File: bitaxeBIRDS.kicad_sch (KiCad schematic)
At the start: 10 parts, among them J1001 XT30

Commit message: started to piece in the BZM2 into schematic
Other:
- sheet Data ports: added none; removed BAP_VIN
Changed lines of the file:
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@@
-	)
-	(junction
-		(at 78.74 44.45)
-		(diameter 0)
-		(color 0 0 0 0)
 	)
 	(junction
@@
 	(wire
 		(pts
-			(xy 78.74 44.45) (xy 102.87 44.45)
+			(xy 58.42 44.45) (xy 102.87 44.45)
 		)
 		(stroke
@@
 	(wire
 		(pts
-			(xy 58.42 44.45) (xy 78.74 44.45)
-		)
-		(stroke
-			(width 0)
-			(type default)
-		)
-	)
-	(wire
-		(pts
 			(xy 90.17 116.84) (xy 102.87 116.84)
 		)
@@
 		(pts
 			(xy 135.89 100.33) (xy 173.99 100.33)
-		)
-		(stroke
-			(width 0)
-			(type default)
-		)
-	)
-	(wire
-		(pts
-			(xy 78.74 124.46) (xy 102.87 124.46)
-		)
-		(stroke
-			(width 0)
-			(type default)
-		)
-	)
-	(wire
-		(pts
-			(xy 78.74 44.45) (xy 78.74 124.46)
 		)
 		(stroke
@@
 			)
 		)
-		(pin "SDA" input
+		(pin "SDA" bidirectional
 			(at 128.27 100.33 0)
 			(effects
@@
 			(effects
 				(font
-					(size 1.27 1.27)
-				)
-				(justify left)
-			)
-		)
-		(pin "BAP_VIN" input
-			(at 102.87 124.46 180)
-			(effects
-				(font

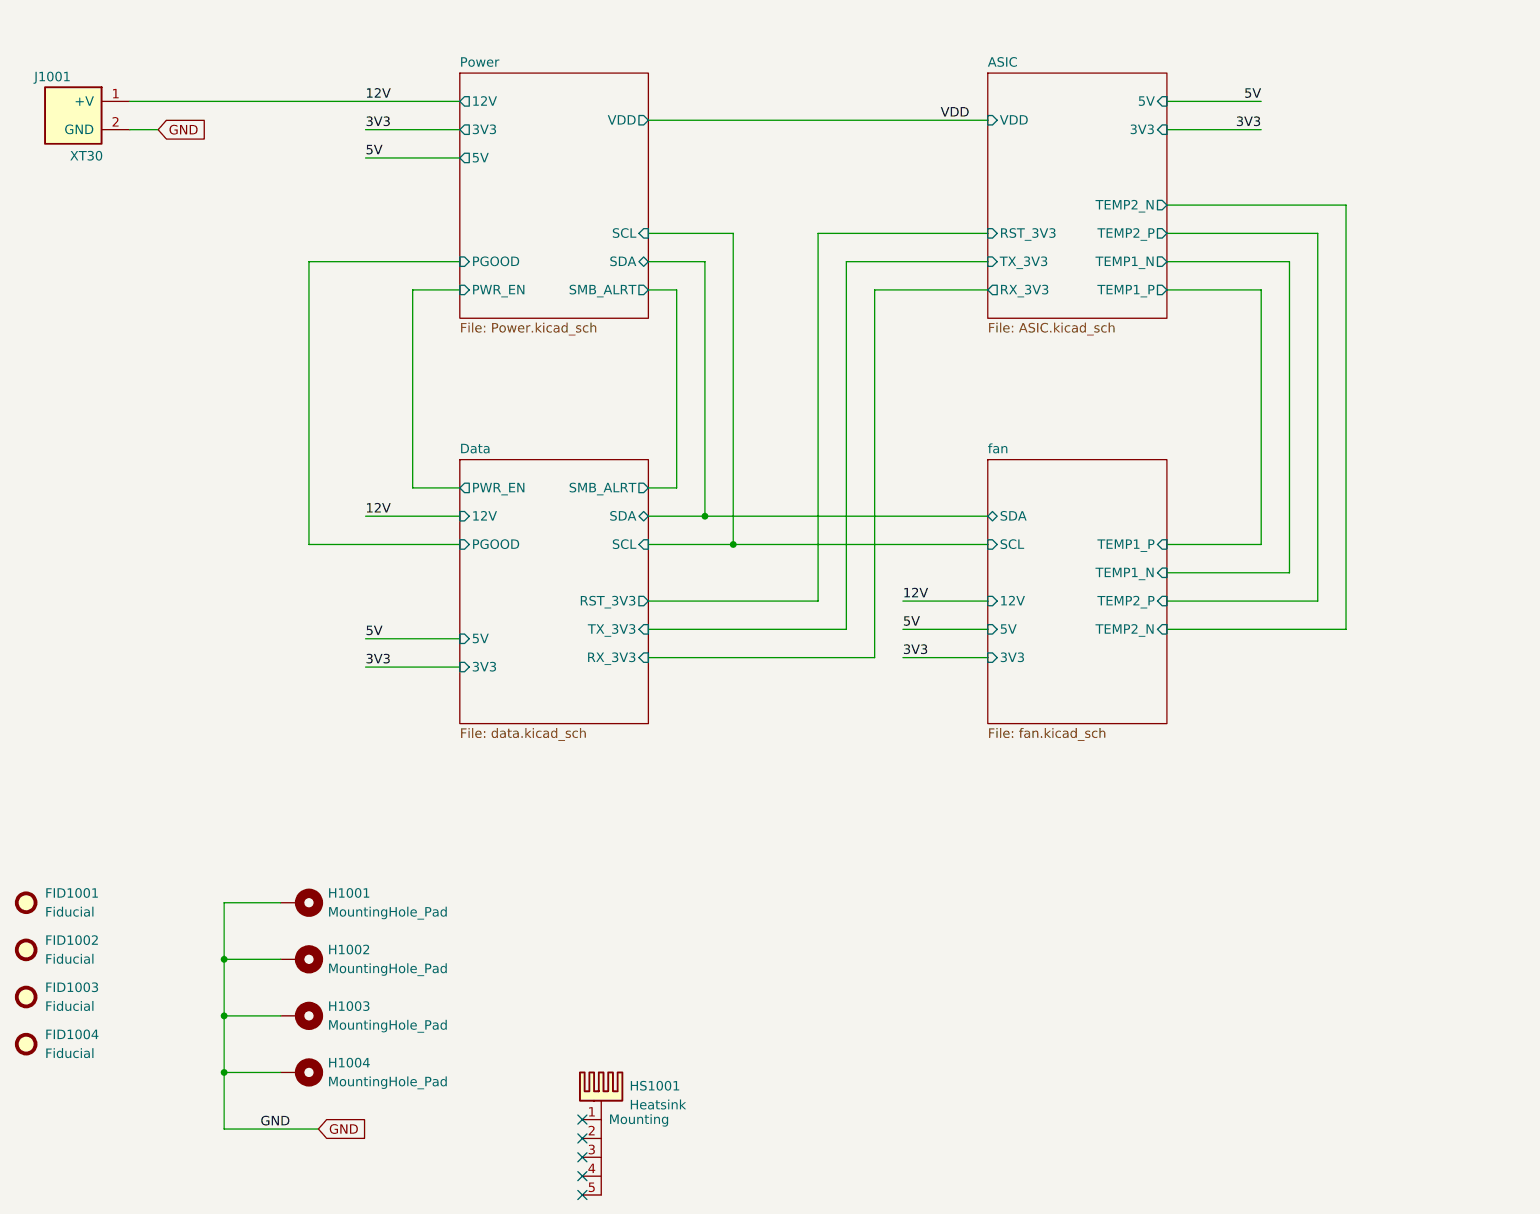
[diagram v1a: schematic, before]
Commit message: finished adding ASICs to schematic. Change VR to single phase 2.8V output
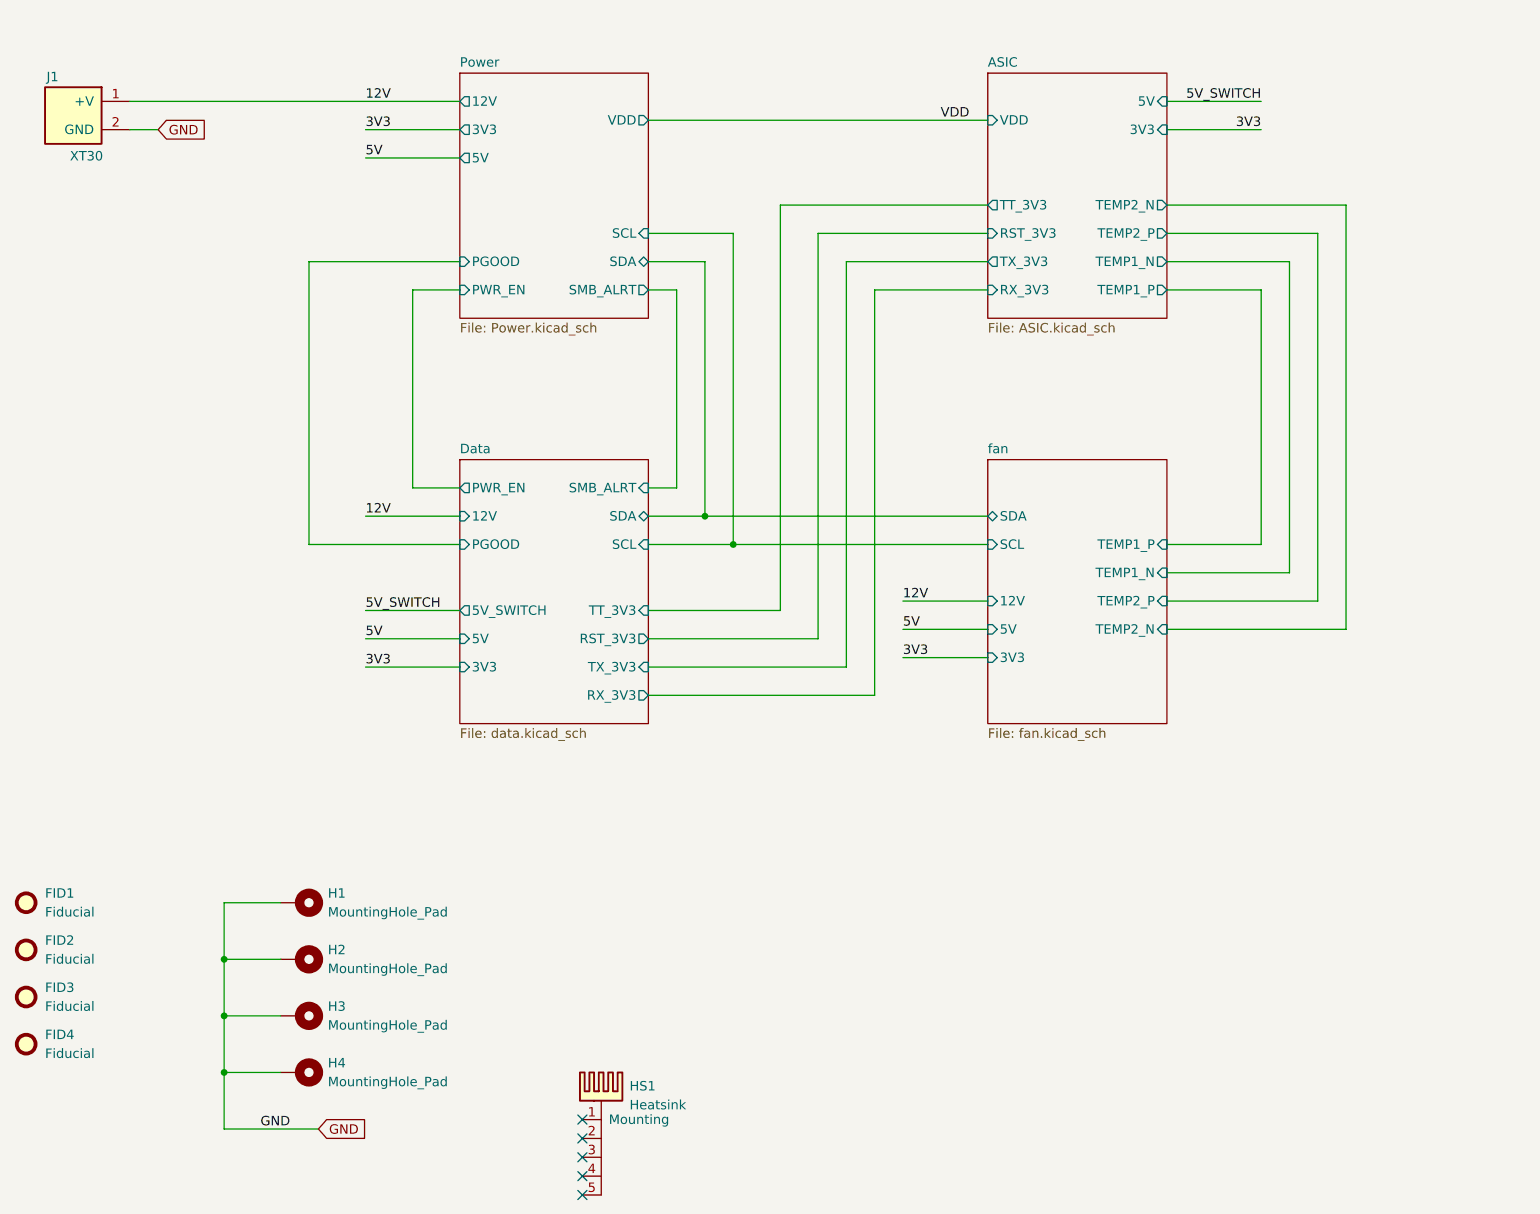
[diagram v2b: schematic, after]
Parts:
- renumbered FID1001 to FID1, FID1002 to FID2, FID1003 to FID3, FID1004 to FID4, H1001 to H1, H1002 to H2, H1003 to H3, H1004 to H4, HS1001 to HS1, J1001 to J1
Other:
- sheet ASIC ports: added TT_3V3; removed none
- sheet Data ports: added 5V_SWITCH, TT_3V3; removed none
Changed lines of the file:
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@@
 	(wire
 		(pts
-			(xy 154.94 115.57) (xy 128.27 115.57)
+			(xy 154.94 120.65) (xy 128.27 120.65)
 		)
 		(stroke
@@
 	(wire
 		(pts
-			(xy 151.13 62.23) (xy 151.13 111.76)
+			(xy 151.13 62.23) (xy 151.13 116.84)
 		)
 		(stroke
@@
 	(wire
 		(pts
+			(xy 128.27 113.03) (xy 146.05 113.03)
+		)
+		(stroke
+			(width 0)
+			(type default)
+		)
+	)
+	(wire
+		(pts
 			(xy 198.12 107.95) (xy 214.63 107.95)
 		)
@@
 	(wire
 		(pts
-			(xy 158.75 69.85) (xy 158.75 119.38)
+			(xy 158.75 69.85) (xy 158.75 124.46)
 		)
 		(stroke
@@
 	(wire
 		(pts
-			(xy 154.94 66.04) (xy 154.94 115.57)
+			(xy 90.17 113.03) (xy 102.87 113.03)
+		)
+		(stroke
+			(width 0)
+			(type default)
+		)
+	)
+	(wire
+		(pts
+			(xy 154.94 66.04) (xy 154.94 120.65)
 		)
 		(stroke
@@
 	(wire
 		(pts
-			(xy 158.75 119.38) (xy 128.27 119.38)
+			(xy 158.75 124.46) (xy 128.27 124.46)
 		)
 		(stroke
@@
 	(wire
 		(pts
+			(xy 146.05 58.42) (xy 146.05 113.03)
+		)
+		(stroke
+			(width 0)
+			(type default)
+		)
+	)
+	(wire
+		(pts
 			(xy 90.17 120.65) (xy 102.87 120.65)
 		)
@@
 	(wire
 		(pts
+			(xy 173.99 58.42) (xy 146.05 58.42)
+		)
+		(stroke
+			(width 0)
+			(type default)
+		)
+	)
+	(wire
+		(pts
 			(xy 71.12 167.64) (xy 71.12 175.26)
 		)
@@
 	(wire
 		(pts
-			(xy 151.13 111.76) (xy 128.27 111.76)
+			(xy 151.13 116.84) (xy 128.27 116.84)
 		)
 		(stroke
@@
 		)
 	)
+	(label "5V_SWITCH"
+		(at 90.17 113.03 0)
+		(effects
+			(font
+				(size 1.27 1.27)
+			)
+			(justify left bottom)
+		)
+	)
 	(label "3V3"
 		(at 162.56 119.38 0)
@@
 		)
 	)
-	(label "5V"
+	(label "5V_SWITCH"
 		(at 210.82 44.45 180)
 		(effects
@@
 		(dnp no)
 		(fields_autoplaced yes)
-		(property "Reference" "H1002"
+		(property "Reference" "H2"
 			(at 85.09 158.7499 90)
 			(effects
@@
 			(project "BitaxeGT"
 				(path "/61fe8d2c-9301-4ad9-8caf-c47acfa835b0"
-					(reference "H1002")
+					(reference "H2")
 					(unit 1)
 				)
@@
 		(dnp no)
 		(fields_autoplaced yes)
-		(property "Reference" "HS1001"
+		(property "Reference" "HS1"
 			(at 125.73 177.1014 0)
 			(effects
@@
 			(project ""
 				(path "/61fe8d2c-9301-4ad9-8caf-c47acfa835b0"
-					(reference "HS1001")
+					(reference "HS1")
 					(unit 1)
 				)
@@
 		(dnp no)
 		(fields_autoplaced yes)
-		(property "Reference" "H1004"
+		(property "Reference" "H4"
 			(at 85.09 173.9899 90)
 			(effects
@@
 			(project "BitaxeGT"
 				(path "/61fe8d2c-9301-4ad9-8caf-c47acfa835b0"
-					(reference "H1004")
+					(reference "H4")
 					(unit 1)
 				)
@@
 		(dnp no)
 		(fields_autoplaced yes)
-		(property "Reference" "H1003"
+		(property "Reference" "H3"
 			(at 85.09 166.3699 90)
 			(effects
@@
 			(project "BitaxeGT"
 				(path "/61fe8d2c-9301-4ad9-8caf-c47acfa835b0"
-					(reference "H1003")
+					(reference "H3")
 					(unit 1)
 				)
@@
 		(on_board yes)
 		(dnp no)
-		(property "Reference" "J1001"
+		(property "Reference" "J1"
 			(at 48.006 41.148 0)
 			(effects
@@
 			(project "BitaxeGT"
 				(path "/61fe8d2c-9301-4ad9-8caf-c47acfa835b0"
-					(reference "J1001")
+					(reference "J1")
 					(unit 1)
 				)
@@
 		(dnp no)
 		(fields_autoplaced yes)
-		(property "Reference" "FID1002"
+		(property "Reference" "FID2"
 			(at 46.99 157.4799 0)
 			(effects
@@
 			(project "BitaxeGT"
 				(path "/61fe8d2c-9301-4ad9-8caf-c47acfa835b0"
-					(reference "FID1002")
+					(reference "FID2")
 					(unit 1)
 				)
@@
 		(dnp no)
 		(fields_autoplaced yes)
-		(property "Reference" "H1001"
+		(property "Reference" "H1"
 			(at 85.09 151.1299 90)
 			(effects
@@
 			(project ""
 				(path "/61fe8d2c-9301-4ad9-8caf-c47acfa835b0"
-					(reference "H1001")
+					(reference "H1")
 					(unit 1)
 				)
@@
 		(dnp no)
 		(fields_autoplaced yes)
-		(property "Reference" "FID1004"
+		(property "Reference" "FID4"
 			(at 46.99 170.1799 0)
 			(effects
@@
 			(project "BitaxeGT"
 				(path "/61fe8d2c-9301-4ad9-8caf-c47acfa835b0"
-					(reference "FID1004")
+					(reference "FID4")
 					(unit 1)
 				)
@@
 		(dnp no)
 		(fields_autoplaced yes)
-		(property "Reference" "FID1001"
+		(property "Reference" "FID1"
 			(at 46.99 151.1299 0)
 			(effects
@@
 			(project ""
 				(path "/61fe8d2c-9301-4ad9-8caf-c47acfa835b0"
-					(reference "FID1001")
+					(reference "FID1")
 					(unit 1)
 				)
@@
 		(dnp no)
 		(fields_autoplaced yes)
-		(property "Reference" "FID1003"
+		(property "Reference" "FID3"
 			(at 46.99 163.8299 0)
 			(effects
@@
 			(project "BitaxeGT"
 				(path "/61fe8d2c-9301-4ad9-8caf-c47acfa835b0"
-					(reference "FID1003")
+					(reference "FID3")
 					(unit 1)
 				)
@@
 			)
 		)
-		(pin "SMB_ALRT" output
+		(pin "SMB_ALRT" input
 			(at 128.27 96.52 0)
 			(effects
@@
 		)
 		(pin "TX_3V3" input
-			(at 128.27 115.57 0)
+			(at 128.27 120.65 0)
 			(effects
 				(font
@@
 			)
 		)
-		(pin "RX_3V3" input
-			(at 128.27 119.38 0)
+		(pin "RX_3V3" output
+			(at 128.27 124.46 0)
 			(effects
 				(font
@@
 		)
 		(pin "RST_3V3" output
-			(at 128.27 111.76 0)
+			(at 128.27 116.84 0)
 			(effects
 				(font
@@
 				)
 				(justify left)
+			)
+		)
+		(pin "5V_SWITCH" output
+			(at 102.87 113.03 180)
+			(effects
+				(font
+					(size 1.27 1.27)
+				)
+				(justify left)
+			)
+		)
+		(pin "TT_3V3" input
+			(at 128.27 113.03 0)
+			(effects
+				(font
+					(size 1.27 1.27)
+				)
+				(justify right)
 			)
 		)
@@
 			)
 		)
-		(pin "TX_3V3" input
+		(pin "TX_3V3" output
 			(at 173.99 66.04 180)
 			(effects
@@
 			)
 		)
-		(pin "RX_3V3" output
+		(pin "RX_3V3" input
 			(at 173.99 69.85 180)
 			(effects
@@
 			)
 		)
+		(pin "TT_3V3" output
+			(at 173.99 58.42 180)
+			(effects
+				(font
+					(size 1.27 1.27)
+				)
+				(justify left)
+			)
+		)

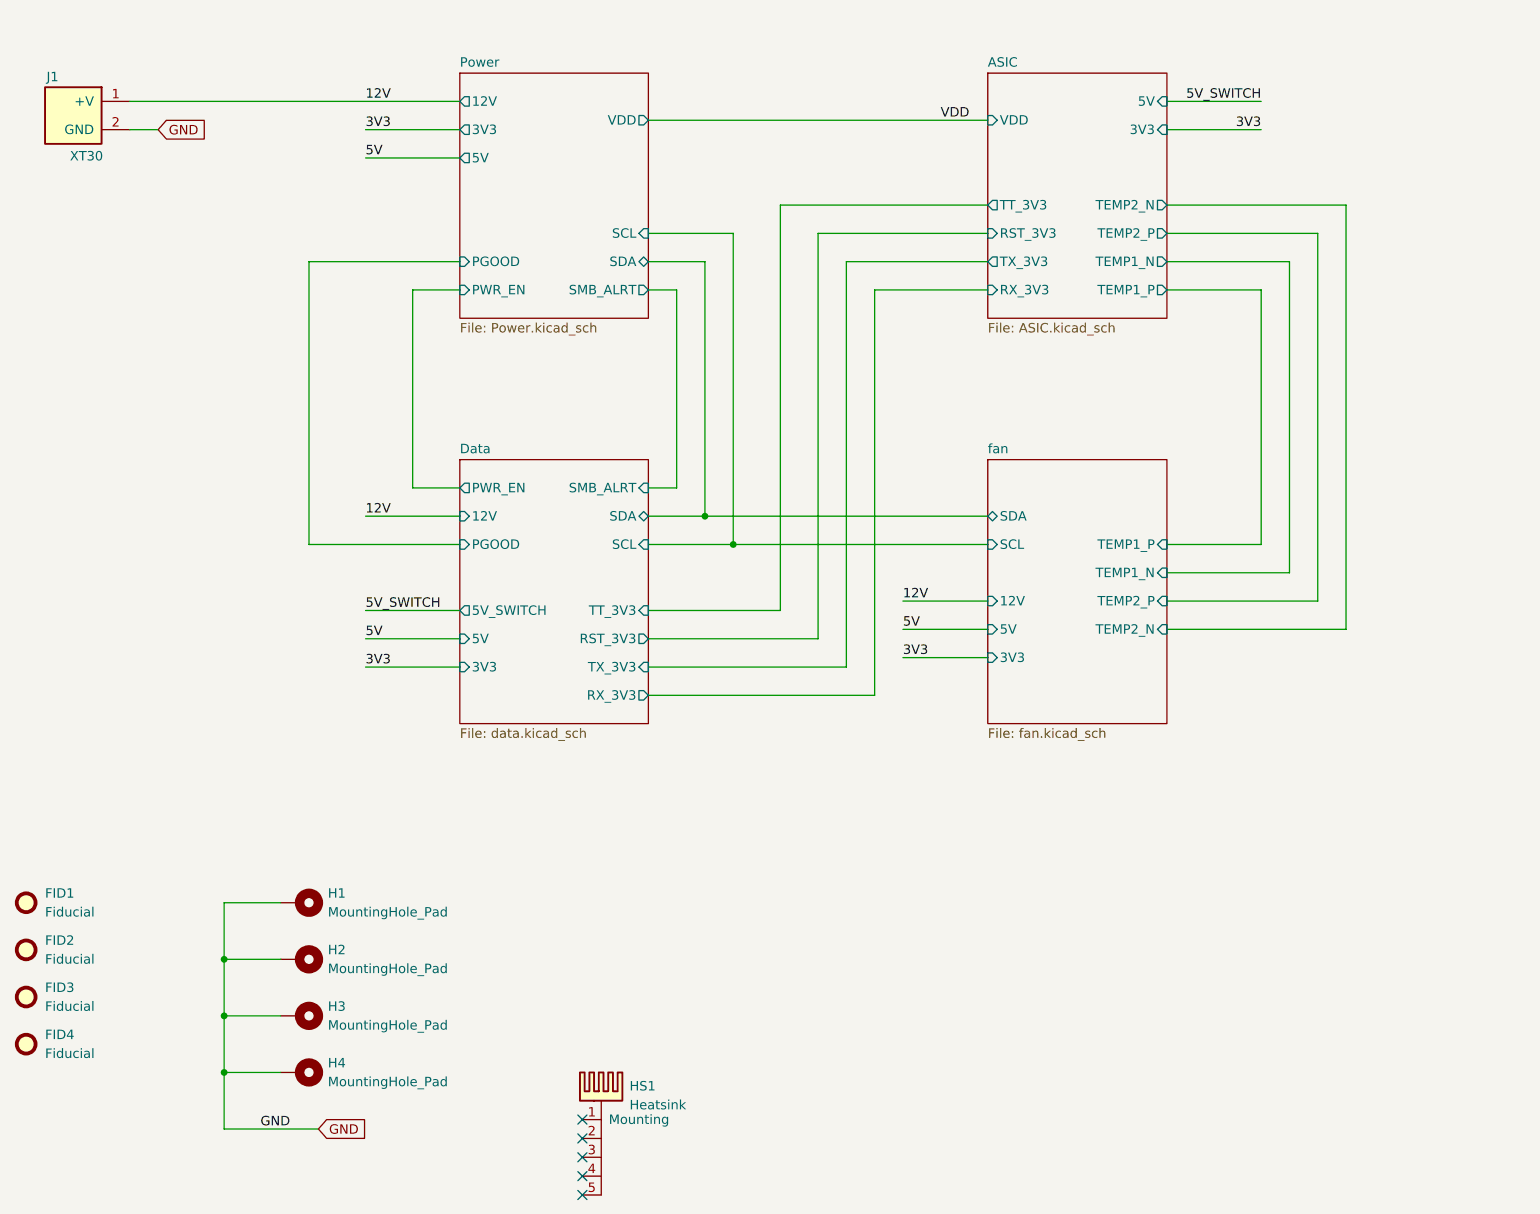
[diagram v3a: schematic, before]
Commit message: Added RP Pico W2 to schematic. Fixed Domain 1-2 level shifter pins. Added test points
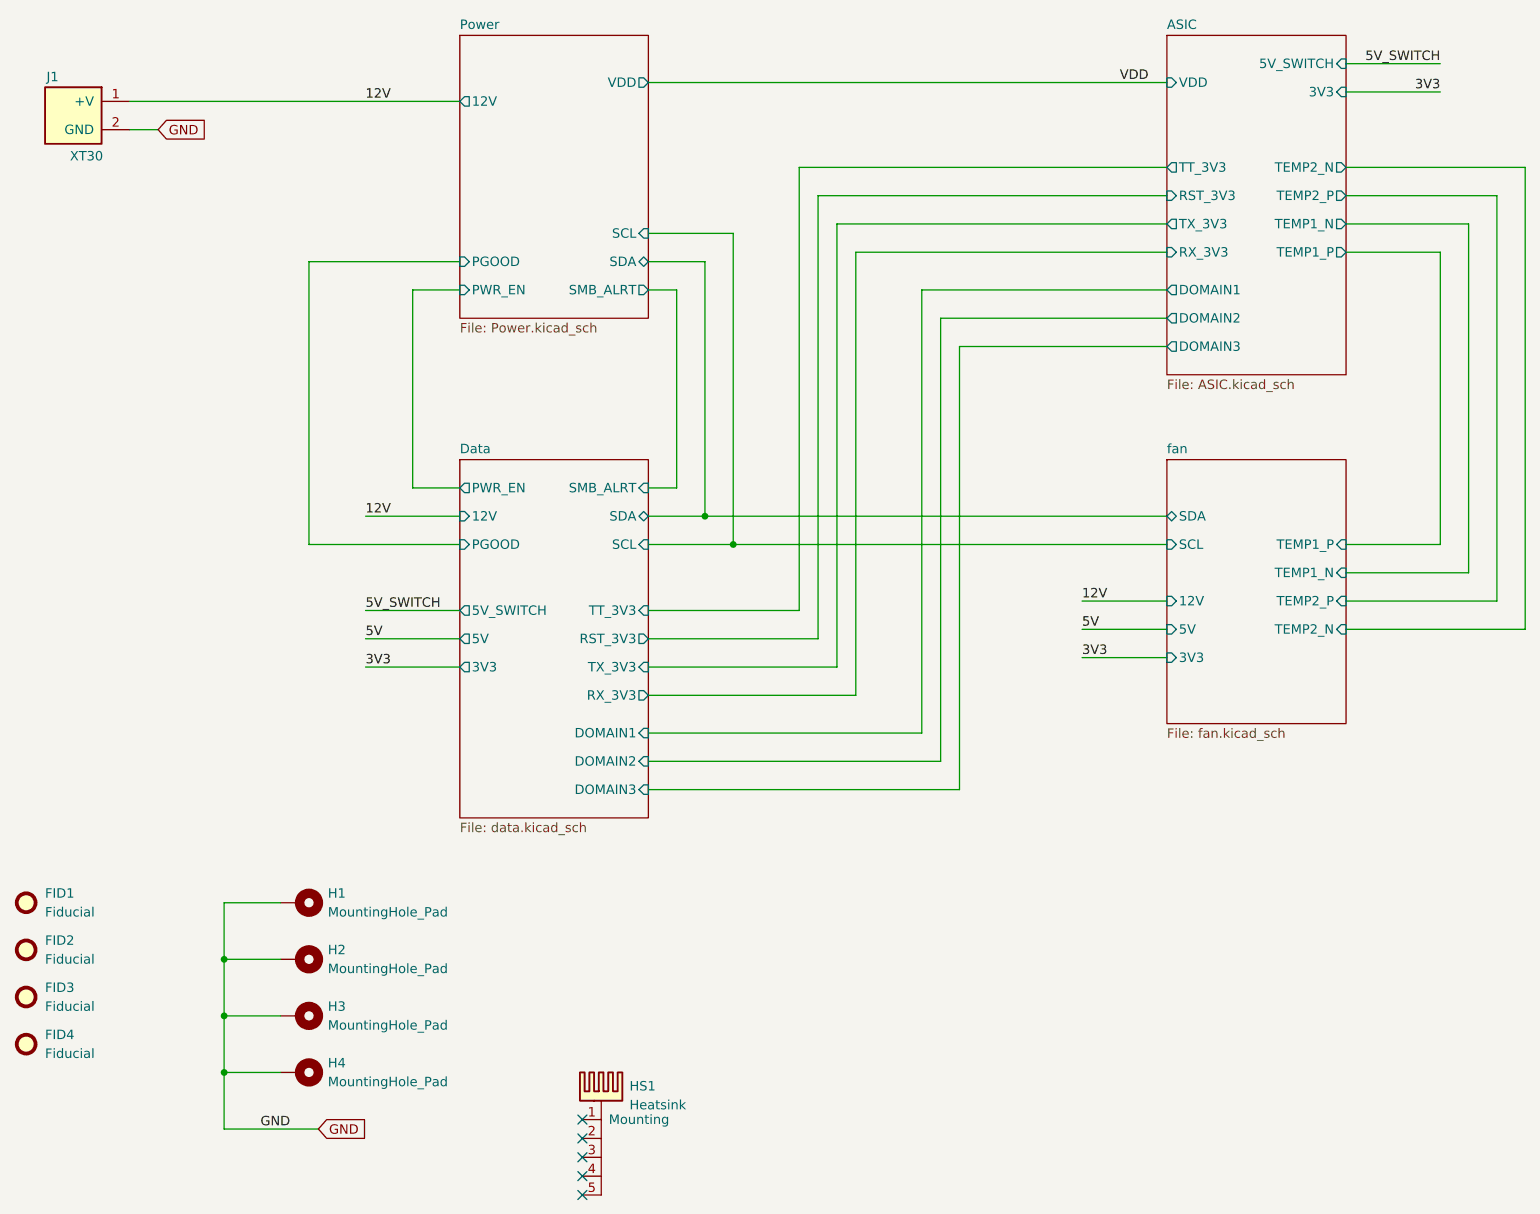
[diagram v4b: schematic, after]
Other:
- sheet ASIC ports: added 5V_SWITCH, DOMAIN1, DOMAIN2, DOMAIN3; removed 5V
- sheet Data ports: added DOMAIN1, DOMAIN2, DOMAIN3; removed none
- sheet Power ports: added none; removed 3V3, 5V
